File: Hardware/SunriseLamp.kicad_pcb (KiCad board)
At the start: 4 copper layers, 80 x 80 mm, 113 parts, among them J1 Molex 047053-1000, J2 S3B-XH-A, J3 Molex 26013114, P1 XT60PW-M, P6 TYPE-C-31-M-12, Q1 MMBT3904, Q2 MMBT3904, Q3 PMV16XNR, Q4 MMBT3904, U1 LM3414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

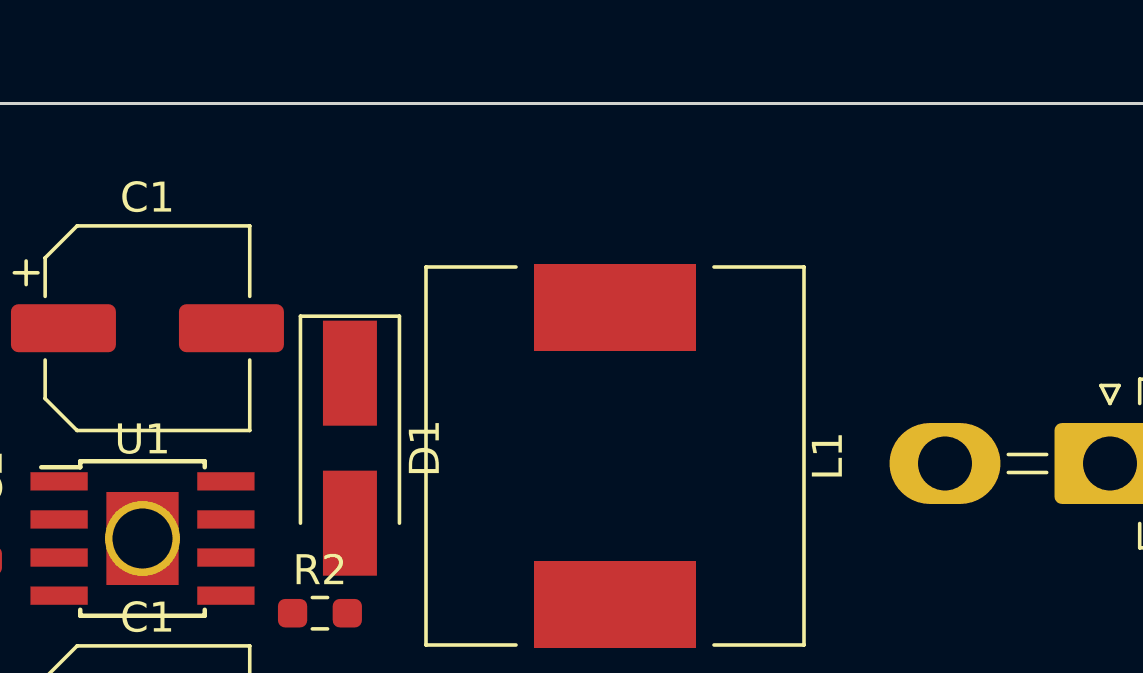
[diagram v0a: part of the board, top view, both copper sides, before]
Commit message: finally created part for pushbutton
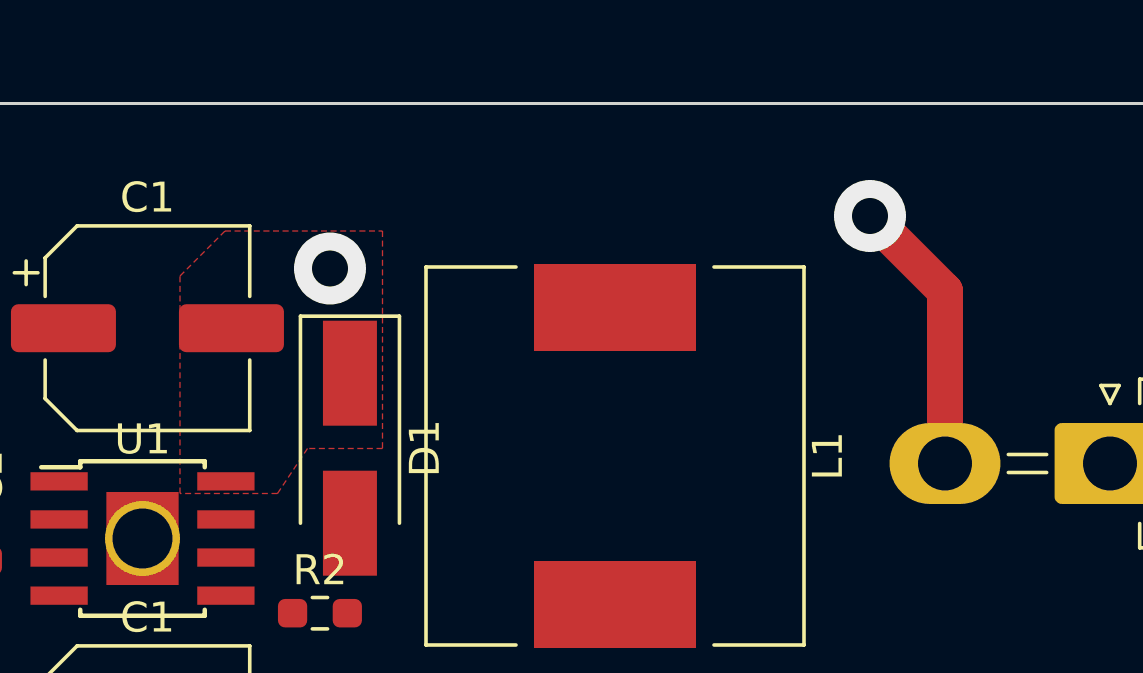
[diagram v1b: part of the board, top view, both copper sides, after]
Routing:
- net +36V: track 0.00 -> 28.0 mm, vias 0 -> 2
- added copper zone on F.Cu, net +36V
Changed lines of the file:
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@@
   (gr_line (start 150 74.25) (end 150 145.75) (layer "Edge.Cuts") (width 0.1))
   (gr_arc (start 150 74.25) (mid 151.244796 71.244796) (end 154.25 70) (layer "Edge.Cuts") (width 0.1))
+  (segment (start 210.25 82) (end 210.25 76.25) (width 1.2) (layer "F.Cu") (net 2))
+  (segment (start 210.25 76.25) (end 207.75 73.75) (width 1.2) (layer "F.Cu") (net 2))
+  (via (at 189.75 75.5) (size 2.4) (drill 1.2) (layers "F.Cu" "B.Cu") (net 2))
+  (via (at 207.75 73.75) (size 2.4) (drill 1.2) (layers "F.Cu" "B.Cu") (remove_unused_layers) (net 2))
+  (segment (start 207.75 73.75) (end 191.5 73.75) (width 1.2) (layer "In1.Cu") (net 2))
+  (segment (start 191.5 73.75) (end 189.75 75.5) (width 1.2) (layer "In1.Cu") (net 2))
+  (zone (net 2) (net_name "+36V") (layer "F.Cu") (hatch edge 0.508)
+    (connect_pads thru_hole_only (clearance 0.508))
+    (min_thickness 0.254)
+    (fill (thermal_gap 0.508) (thermal_bridge_width 0.508))
+    (polygon
+      (pts
+        (xy 191.5 81.5)
+        (xy 189 81.5)
+        (xy 188 83)
+        (xy 184.75 83)
+        (xy 184.75 75.75)
+        (xy 186.25 74.25)
+        (xy 191.5 74.25)
+      )
+    )
+  )
   (group "" (id 11212e92-3e2e-410b-89a6-76a62df9e31c)
     (members

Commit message: updated to new KiCAD format
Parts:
- moved C22 610.5 mm to (93.0, 245.8)
- moved C23 610.5 mm to (108.3, 245.8)
